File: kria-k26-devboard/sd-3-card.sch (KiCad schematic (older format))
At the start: 20 parts, among them J2 1140084168, Q1 BSS123, Q2 AO3401A, U5 NVT4858HKZ, U6 TPS2116DRLR

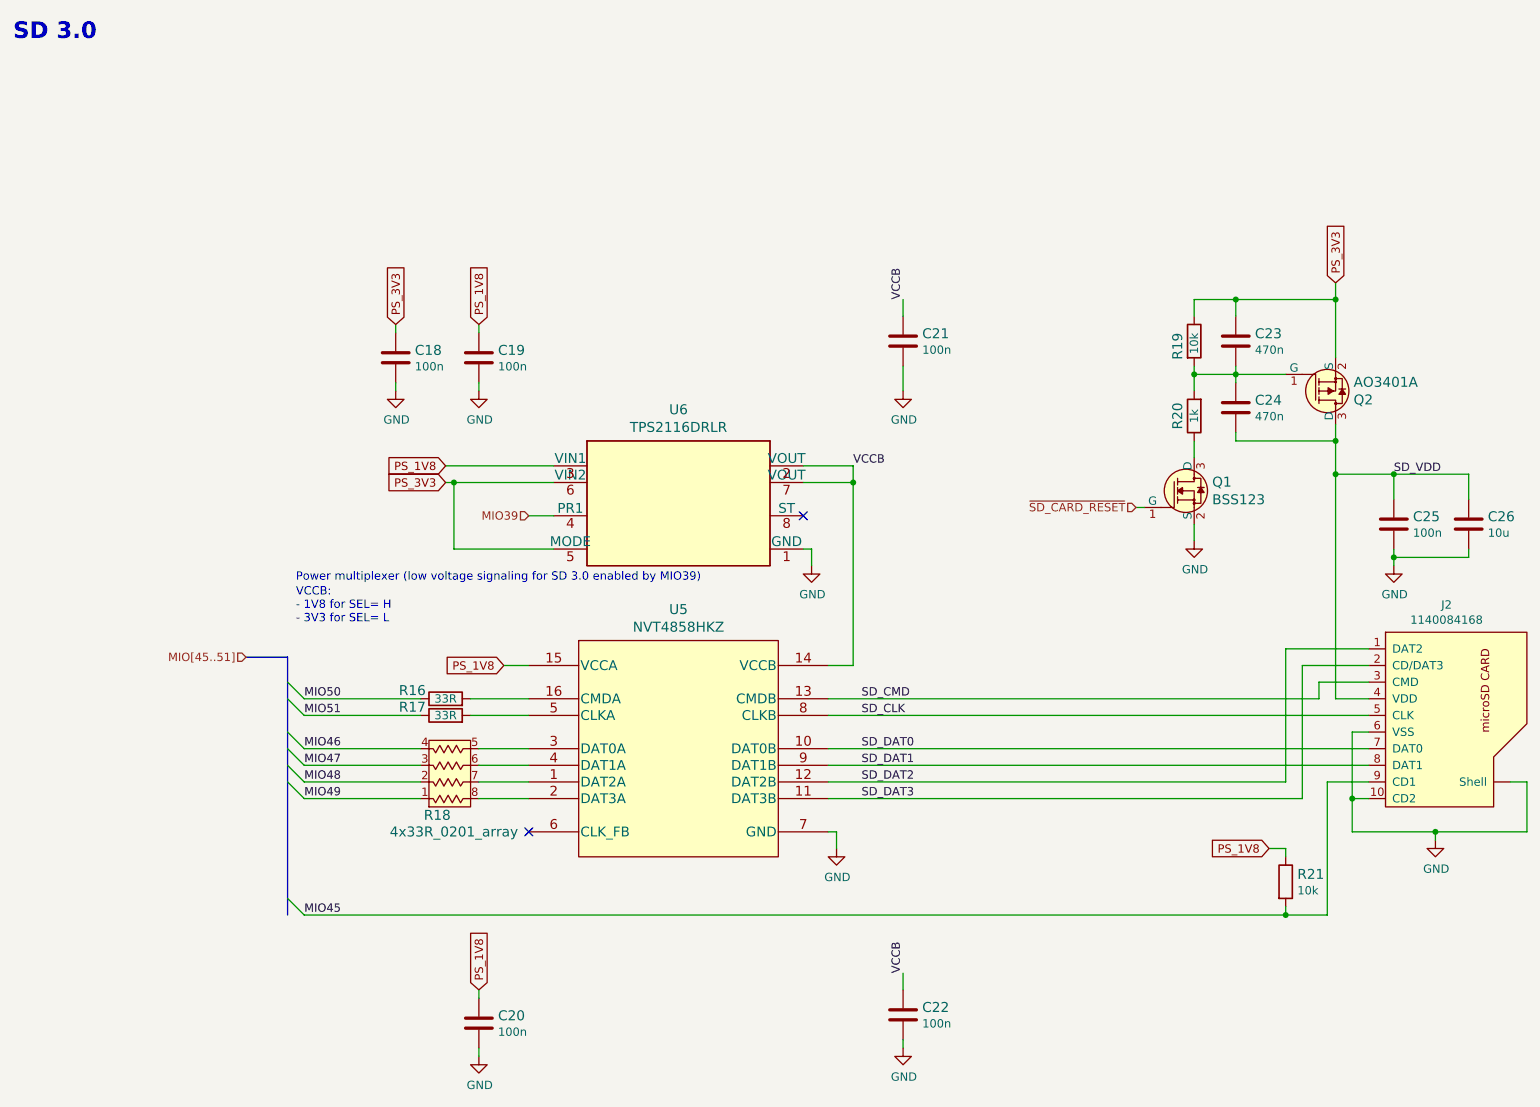
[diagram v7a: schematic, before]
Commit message: Replaced 4A DC-DC conventer, finished cleaning after replacement
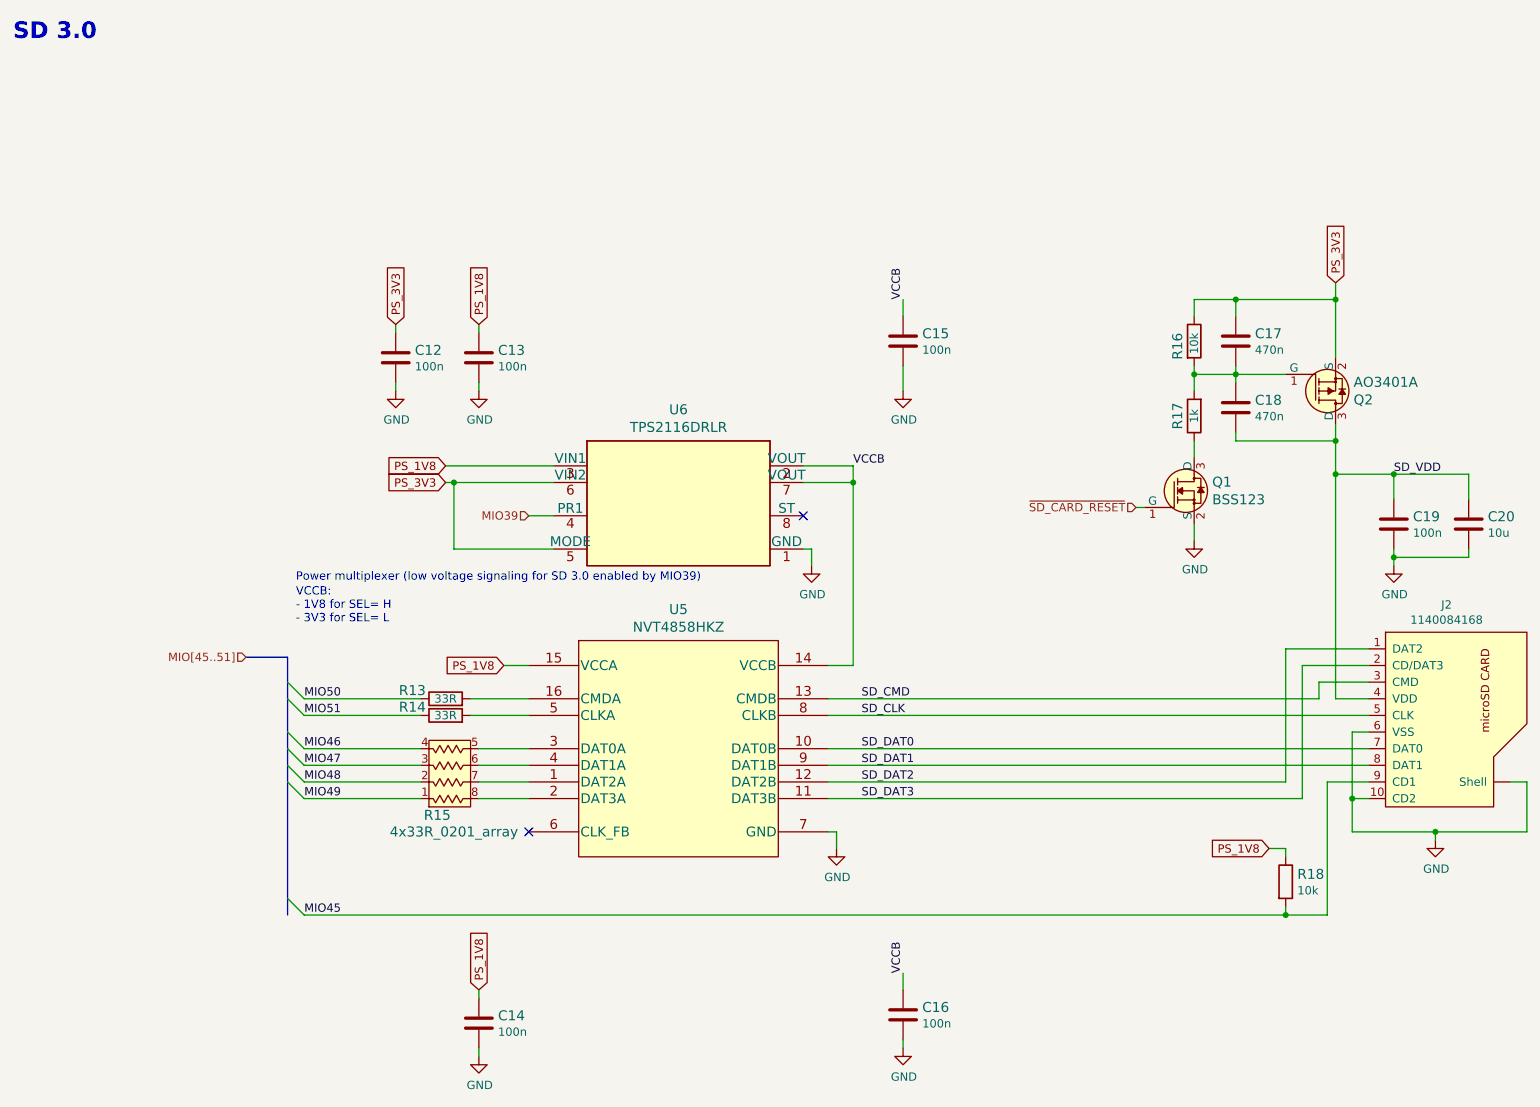
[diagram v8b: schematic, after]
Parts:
- renumbered C18 to C12, C19 to C13, C20 to C14, C21 to C15, C22 to C16, C23 to C17, C24 to C18, C25 to C19, C26 to C20, R16 to R13, R17 to R14, R18 to R15, R19 to R16, R20 to R17, R21 to R18
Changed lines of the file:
@@
 Connection ~ 5650 3400
 $Comp
-L power:GND #PWR032
+L power:GND #PWR027
 U 1 1 631D2E7A
 P 5400 3900
-F 0 "#PWR032" H 5400 3650 50  0001 C CNN
+F 0 "#PWR027" H 5400 3650 50  0001 C CNN
 F 1 "GND" H 5405 3727 50  0000 C CNN
 F 2 "" H 5400 3900 50  0001 C CNN
@@
 	3550 4500 3700 4500
 $Comp
-L antmicroResistors0402:R_33R_0402 R17
+L antmicroResistors0402:R_33R_0402 R14
 U 1 1 631DF31D
 P 3200 4800
-F 0 "R17" H 3000 4850 60  0000 C CNN
+F 0 "R14" H 3000 4850 60  0000 C CNN
 F 1 "R_33R_0402" H 3200 4650 60  0001 C CNN
 F 2 "antmicro-footprints:0402-res" H 3400 5000 60  0001 L CNN
@@
 $EndComp
 $Comp
-L antmicroResistors0402:R_33R_0402 R16
+L antmicroResistors0402:R_33R_0402 R13
 U 1 1 631E087B
 P 3200 4700
-F 0 "R16" H 3000 4750 60  0000 C CNN
+F 0 "R13" H 3000 4750 60  0000 C CNN
 F 1 "R_33R_0402" H 3200 4550 60  0001 C CNN
 F 2 "antmicro-footprints:0402-res" H 3400 4900 60  0001 L CNN
@@
 	8450 4600 8750 4600
 $Comp
-L power:GND #PWR033
+L power:GND #PWR028
 U 1 1 631E6AA8
 P 5550 5600
-F 0 "#PWR033" H 5550 5350 50  0001 C CNN
+F 0 "#PWR028" H 5550 5350 50  0001 C CNN
 F 1 "GND" H 5555 5427 50  0000 C CNN
 F 2 "" H 5550 5600 50  0001 C CNN
@@
 PS_3V3
 $Comp
-L antmicroCapacitors0402:C_100n_0402 C18
+L antmicroCapacitors0402:C_100n_0402 C12
 U 1 1 631F0D3B
 P 2900 2650
-F 0 "C18" H 3015 2695 60  0000 L CNN
+F 0 "C12" H 3015 2695 60  0000 L CNN
 F 1 "C_100n_0402" H 2900 2500 60  0001 C CNN
 F 2 "antmicro-footprints:0402-cap" H 3100 2850 60  0001 L CNN
@@
 $EndComp
 $Comp
-L antmicroCapacitors0402:C_100n_0402 C19
+L antmicroCapacitors0402:C_100n_0402 C13
 U 1 1 631F1104
 P 3400 2650
-F 0 "C19" H 3515 2695 60  0000 L CNN
+F 0 "C13" H 3515 2695 60  0000 L CNN
 F 1 "C_100n_0402" H 3400 2500 60  0001 C CNN
 F 2 "antmicro-footprints:0402-cap" H 3600 2850 60  0001 L CNN
@@
 $EndComp
 $Comp
-L antmicroCapacitors0402:C_100n_0402 C21
+L antmicroCapacitors0402:C_100n_0402 C15
 U 1 1 631F1457
 P 5950 2550
-F 0 "C21" H 6065 2595 60  0000 L CNN
+F 0 "C15" H 6065 2595 60  0000 L CNN
 F 1 "C_100n_0402" H 5950 2400 60  0001 C CNN
 F 2 "antmicro-footprints:0402-cap" H 6150 2750 60  0001 L CNN
@@
 	3400 2500 3400 2450
 $Comp
-L power:GND #PWR029
+L power:GND #PWR024
 U 1 1 63200563
 P 2900 2850
-F 0 "#PWR029" H 2900 2600 50  0001 C CNN
+F 0 "#PWR024" H 2900 2600 50  0001 C CNN
 F 1 "GND" H 2905 2677 50  0000 C CNN
 F 2 "" H 2900 2850 50  0001 C CNN
@@
 MIO39
 $Comp
-L antmicroCapacitors0402:C_100n_0402 C25
+L antmicroCapacitors0402:C_100n_0402 C19
 U 1 1 6323158C
 P 8900 3650
-F 0 "C25" H 9015 3695 60  0000 L CNN
+F 0 "C19" H 9015 3695 60  0000 L CNN
 F 1 "C_100n_0402" H 8900 3500 60  0001 C CNN
 F 2 "antmicro-footprints:0402-cap" H 9100 3850 60  0001 L CNN
@@
 	8900 3900 8900 3850
 $Comp
-L antmicroCapacitors0603:C_10u_0603 C26
+L antmicroCapacitors0603:C_10u_0603 C20
 U 1 1 632347EF
 P 9350 3650
-F 0 "C26" H 9465 3695 60  0000 L CNN
+F 0 "C20" H 9465 3695 60  0000 L CNN
 F 1 "C_10u_0603" H 9350 3500 60  0001 C CNN
 F 2 "antmicro-footprints:0603-cap" H 9550 3850 60  0001 L CNN
@@
 Connection ~ 8900 3350
 $Comp
-L power:GND #PWR037
+L power:GND #PWR032
 U 1 1 632316CE
 P 8900 3900
-F 0 "#PWR037" H 8900 3650 50  0001 C CNN
+F 0 "#PWR032" H 8900 3650 50  0001 C CNN
 F 1 "GND" H 8905 3727 50  0000 C CNN
 F 2 "" H 8900 3900 50  0001 C CNN
@@
 	5950 2400 5950 2300
 $Comp
-L power:GND #PWR030
+L power:GND #PWR025
 U 1 1 63203F42
 P 3400 2850
-F 0 "#PWR030" H 3400 2600 50  0001 C CNN
+F 0 "#PWR025" H 3400 2600 50  0001 C CNN
 F 1 "GND" H 3405 2677 50  0000 C CNN
 F 2 "" H 3400 2850 50  0001 C CNN
@@
 $EndComp
 $Comp
-L power:GND #PWR034
+L power:GND #PWR029
 U 1 1 63278518
 P 5950 2850
-F 0 "#PWR034" H 5950 2600 50  0001 C CNN
+F 0 "#PWR029" H 5950 2600 50  0001 C CNN
 F 1 "GND" H 5955 2677 50  0000 C CNN
 F 2 "" H 5950 2850 50  0001 C CNN
@@
 	9700 5500 9150 5500
 $Comp
-L power:GND #PWR038
+L power:GND #PWR033
 U 1 1 632822AB
 P 9150 5550
-F 0 "#PWR038" H 9150 5300 50  0001 C CNN
+F 0 "#PWR033" H 9150 5300 50  0001 C CNN
 F 1 "GND" H 9155 5377 50  0000 C CNN
 F 2 "" H 9150 5550 50  0001 C CNN
@@
 $EndComp
 $Comp
-L power:GND #PWR036
+L power:GND #PWR031
 U 1 1 66661087
 P 7700 3750
-F 0 "#PWR036" H 7700 3500 50  0001 C CNN
+F 0 "#PWR031" H 7700 3500 50  0001 C CNN
 F 1 "GND" H 7705 3577 50  0000 C CNN
 F 2 "" H 7700 3750 50  0001 C CNN
@@
 	7700 2300 7700 2400
 $Comp
-L antmicroResistors0402:R_1k_0402 R20
+L antmicroResistors0402:R_1k_0402 R17
 U 1 1 66639BBE
 P 7700 3000
-F 0 "R20" H 7700 3100 60  0000 C CNN
+F 0 "R17" H 7700 3100 60  0000 C CNN
 F 1 "R_1k_0402" H 7700 2850 60  0001 C CNN
 F 2 "antmicro-footprints:0402-res" H 7900 3200 60  0001 L CNN
@@
 $EndComp
 $Comp
-L antmicroCapacitors0402:C_470n_0402 C23
+L antmicroCapacitors0402:C_470n_0402 C17
 U 1 1 666642E9
 P 7950 2550
-F 0 "C23" H 8065 2595 60  0000 L CNN
+F 0 "C17" H 8065 2595 60  0000 L CNN
 F 1 "C_470n_0402" H 7950 2400 60  0001 C CNN
 F 2 "antmicro-footprints:0402-cap" H 8150 2750 60  0001 L CNN
@@
 $EndComp
 $Comp
-L antmicroResistors0402:R_10k_0402 R19
+L antmicroResistors0402:R_10k_0402 R16
 U 1 1 6667AA59
 P 7700 2550
-F 0 "R19" H 7650 2450 60  0000 L CNN
+F 0 "R16" H 7650 2450 60  0000 L CNN
 F 1 "R_10k_0402" H 7700 2400 60  0001 C CNN
 F 2 "antmicro-footprints:0402-res" H 7900 2750 60  0001 L CNN
@@
 ~SD_CARD_RESET
 $Comp
-L antmicroCapacitors0402:C_470n_0402 C24
+L antmicroCapacitors0402:C_470n_0402 C18
 U 1 1 667B7A84
 P 7950 2950
-F 0 "C24" H 8065 2995 60  0000 L CNN
+F 0 "C18" H 8065 2995 60  0000 L CNN
 F 1 "C_470n_0402" H 7950 2800 60  0001 C CNN
 F 2 "antmicro-footprints:0402-cap" H 8150 3150 60  0001 L CNN
@@
 	8550 2300 8550 2650
 $Comp
-L antmicroResistors0402:R_10k_0402 R21
+L antmicroResistors0402:R_10k_0402 R18
 U 1 1 63286775
 P 8250 5800
-F 0 "R21" V 8205 5870 60  0000 L CNN
+F 0 "R18" V 8205 5870 60  0000 L CNN
 F 1 "R_10k_0402" H 8250 5650 60  0001 C CNN
 F 2 "antmicro-footprints:0402-res" H 8450 6000 60  0001 L CNN
@@
 PS_1V8
 $Comp
-L antmicroCapacitors0402:C_100n_0402 C20
+L antmicroCapacitors0402:C_100n_0402 C14
 U 1 1 6986927B
 P 3400 6650
-F 0 "C20" H 3515 6695 60  0000 L CNN
+F 0 "C14" H 3515 6695 60  0000 L CNN
 F 1 "C_100n_0402" H 3400 6500 60  0001 C CNN
 F 2 "antmicro-footprints:0402-cap" H 3600 6850 60  0001 L CNN
@@
 	3400 6850 3400 6800
 $Comp
-L power:GND #PWR031
+L power:GND #PWR026
 U 1 1 69869287
 P 3400 6850
-F 0 "#PWR031" H 3400 6600 50  0001 C CNN
+F 0 "#PWR026" H 3400 6600 50  0001 C CNN
 F 1 "GND" H 3405 6677 50  0000 C CNN
 F 2 "" H 3400 6850 50  0001 C CNN
@@
 $EndComp
 $Comp
-L antmicroCapacitors0402:C_100n_0402 C22
+L antmicroCapacitors0402:C_100n_0402 C16
 U 1 1 69871ED9
 P 5950 6600
-F 0 "C22" H 6065 6645 60  0000 L CNN
+F 0 "C16" H 6065 6645 60  0000 L CNN
 F 1 "C_100n_0402" H 5950 6450 60  0001 C CNN
 F 2 "antmicro-footprints:0402-cap" H 6150 6800 60  0001 L CNN
@@
 	5950 6450 5950 6350
 $Comp
-L power:GND #PWR035
+L power:GND #PWR030
 U 1 1 6987213A
 P 5950 6800
-F 0 "#PWR035" H 5950 6550 50  0001 C CNN
+F 0 "#PWR030" H 5950 6550 50  0001 C CNN
 F 1 "GND" H 5955 6627 50  0000 C CNN
 F 2 "" H 5950 6800 50  0001 C CNN
@@
 SD_CLK
 $Comp
-L antmicroResistorNetworksArrays:4x33R_0201_array R18
+L antmicroResistorNetworksArrays:4x33R_0201_array R15
 U 1 1 632D3168
 P 3250 4900
-F 0 "R18" H 3150 5400 60  0000 C CNN
+F 0 "R15" H 3150 5400 60  0000 C CNN
 F 1 "4x33R_0201_array" H 3250 5500 60  0000 C CNN
 F 2 "antmicro-footprints:EXB18V" H 3050 5650 60  0001 L CNN
